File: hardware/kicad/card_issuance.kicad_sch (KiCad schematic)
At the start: 0 parts

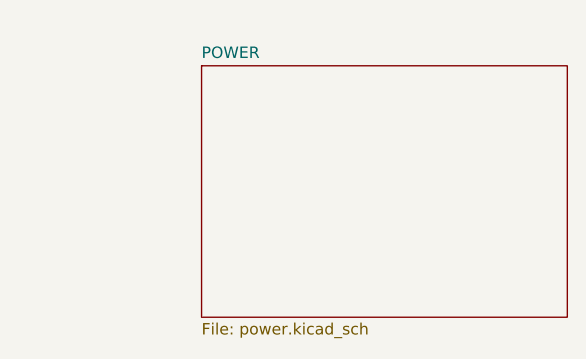
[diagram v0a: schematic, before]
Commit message: fix: protection circuit - MOSFET & enable config
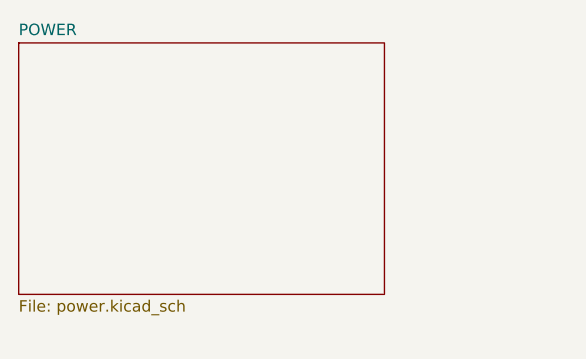
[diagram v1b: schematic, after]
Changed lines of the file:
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@@
 	(paper "A4")
 	(sheet
-		(at 91.44 68.58)
+		(at 71.12 66.04)
 		(size 40.64 27.94)
 		(exclude_from_sim no)
@@
 		)
 		(property "Sheetname" "POWER"
-			(at 91.44 67.8684 0)
+			(at 71.12 65.3284 0)
 			(effects
 				(font
@@
 		)
 		(property "Sheetfile" "power.kicad_sch"
-			(at 91.44 97.1046 0)
+			(at 71.12 94.5646 0)
 			(effects
 				(font

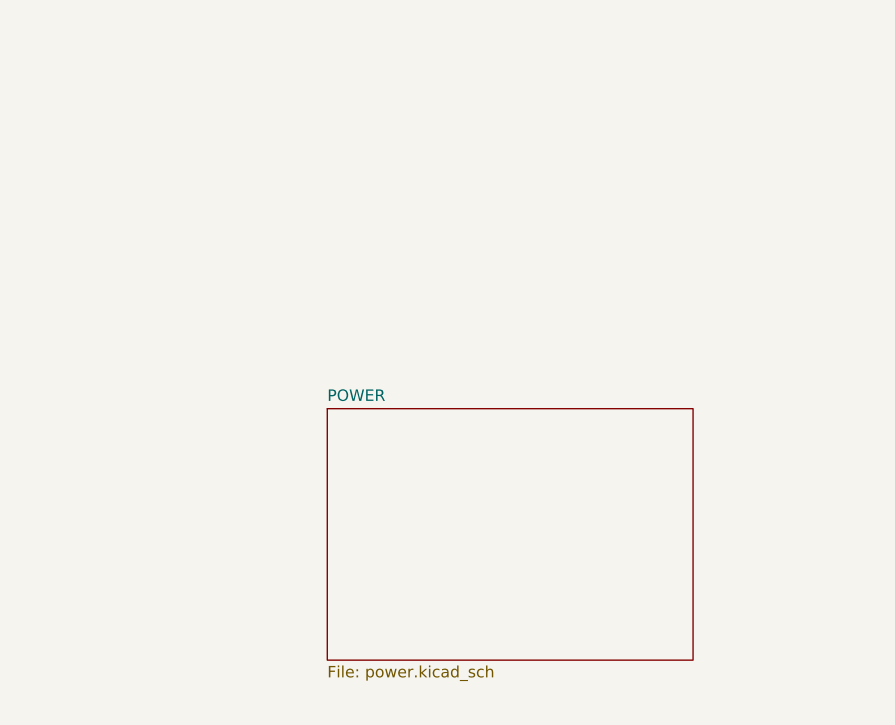
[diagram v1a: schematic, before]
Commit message: feat: separated modules but added power module
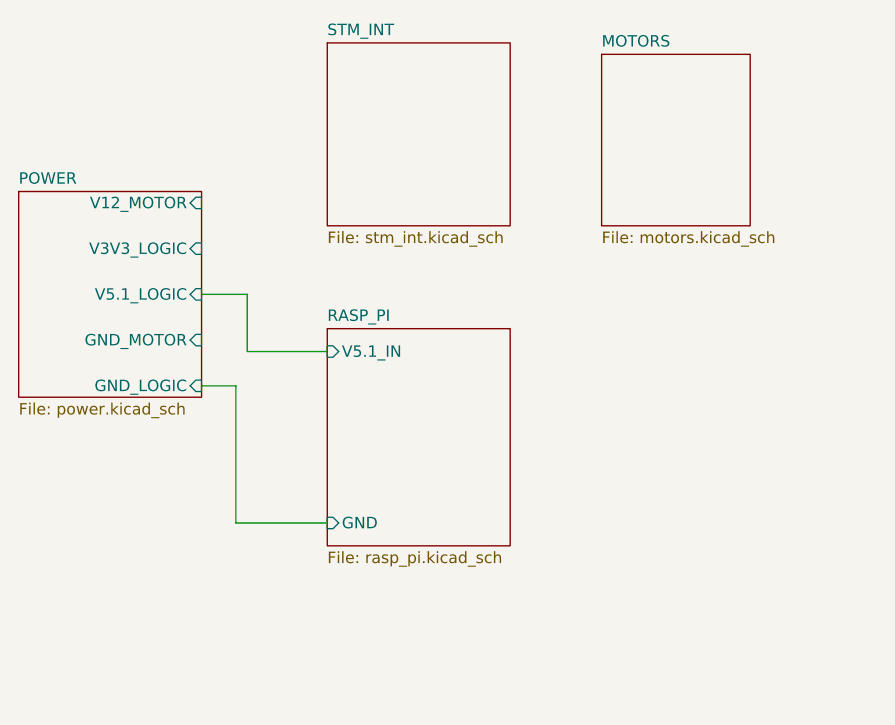
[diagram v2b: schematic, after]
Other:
- added sheet MOTORS (motors.kicad_sch)
- added sheet RASP_PI (rasp_pi.kicad_sch)
- added sheet STM_INT (stm_int.kicad_sch)
- sheet POWER ports: added GND_LOGIC, GND_MOTOR, V12_MOTOR, V3V3_LOGIC, V5.1_LOGIC; removed none
